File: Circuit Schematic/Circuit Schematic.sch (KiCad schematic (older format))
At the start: 7 parts, among them M1 Motor_Servo, M2 Motor_Servo, U1 SM5420E, U2 SM5420E, U3 ABPDJJ

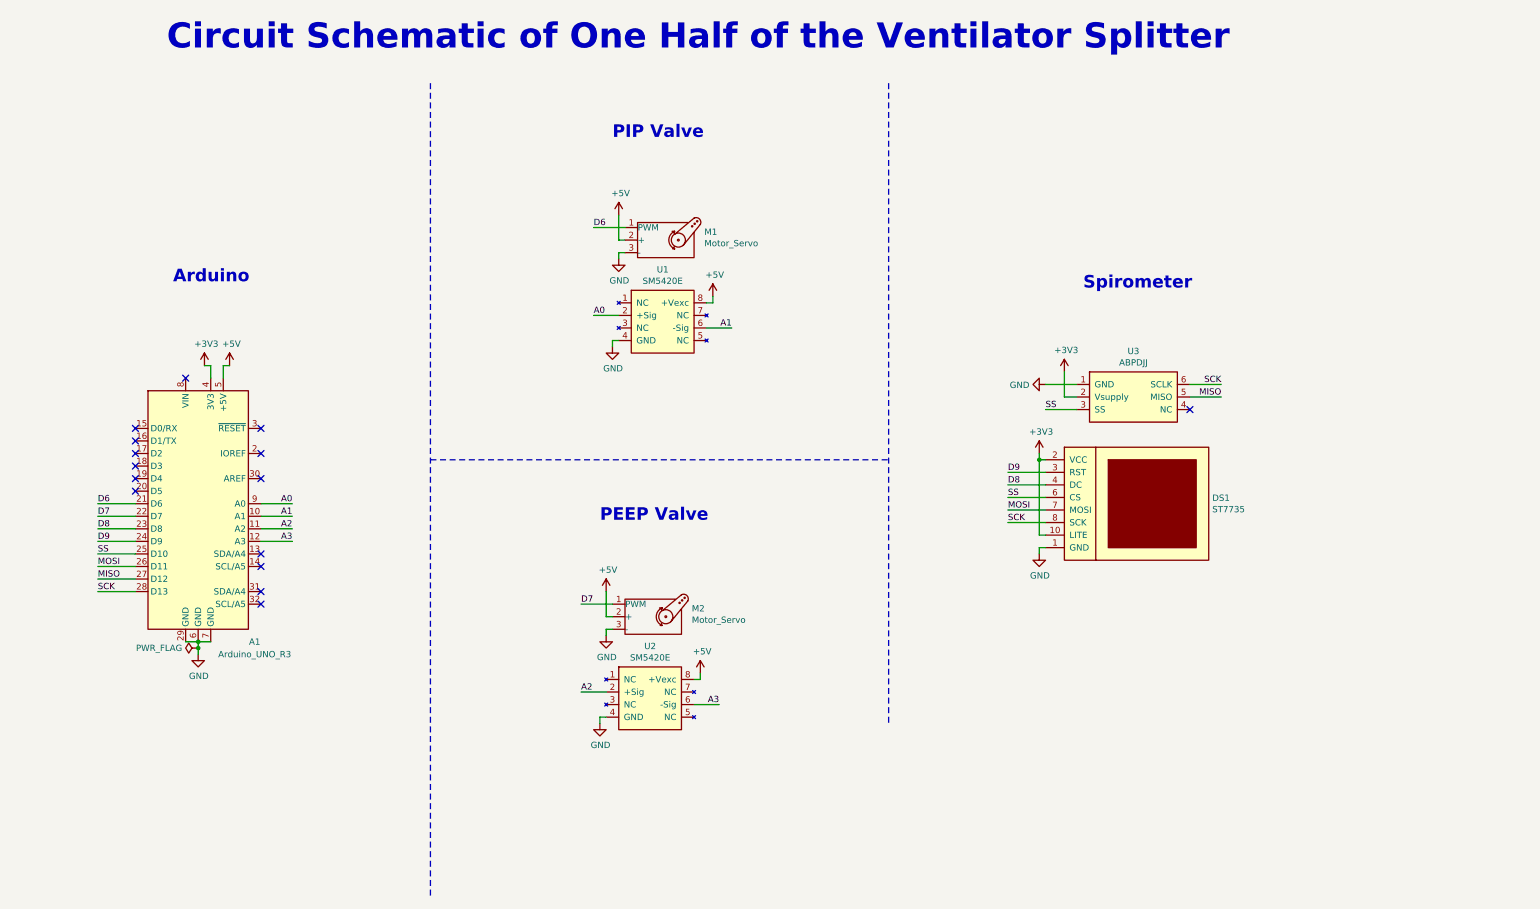
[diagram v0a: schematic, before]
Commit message: Updates schematic to include bluetooth module and alarm system components
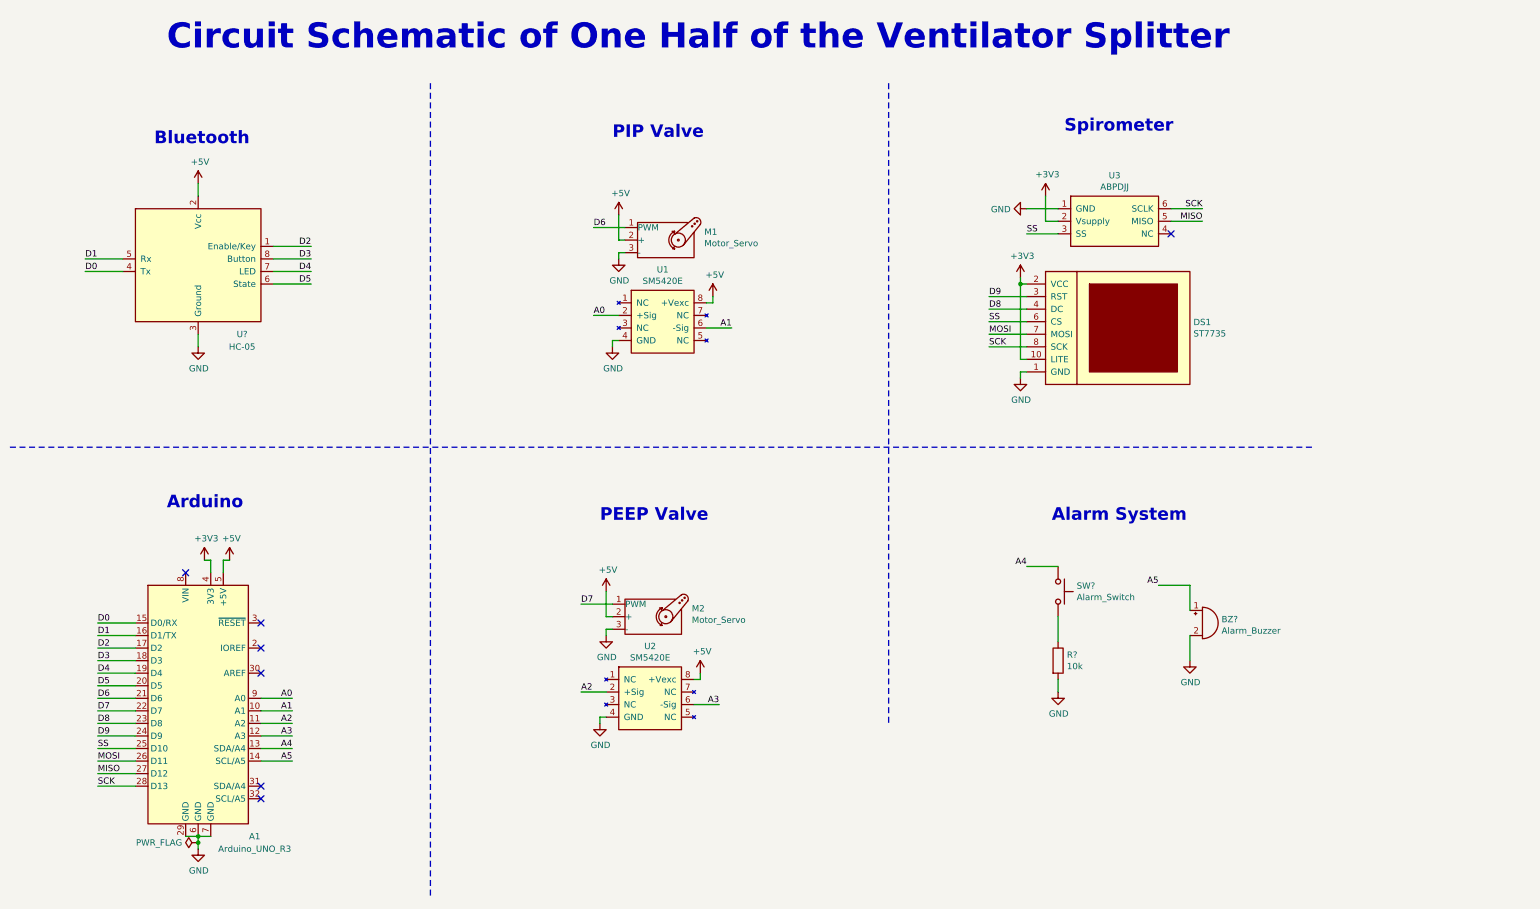
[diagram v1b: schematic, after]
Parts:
- added BZ?: Alarm_Buzzer, symbol Device:Buzzer
- added R?: 10k, symbol Device:R
- added SW?: Alarm_Switch, symbol Switch:SW_Push
- added U?: HC-05, symbol Ventilator-Splitter:HC-05
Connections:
- net +5V: now also U?.2 (Vcc)
- net GND: now also BZ?.2 (+), R?.2, U?.3 (Ground)
- net A4: now reaches A1.13 (SDA/A4)
- net A4: now also SW?.1
- net A5: now reaches A1.14 (SCL/A5)
- net A5: now also BZ?.1 (-)
- net D0: now reaches A1.15 (D0/RX)
- net D0: now also U?.4 (Tx)
- net D1: now reaches A1.16 (D1/TX)
- net D1: now also U?.5 (Rx)
- net D2: now reaches A1.17 (D2)
- net D2: now also U?.1 (Enable/Key)
- net D3: now reaches A1.18 (D3)
- net D3: now also U?.8 (Button)
- net D4: now reaches A1.19 (D4)
- net D4: now also U?.7 (LED)
- net D5: now reaches A1.20 (D5)
- net D5: now also U?.6 (State)
- new net: R?.1, SW?.2
- no-connect marks 15 -> 7
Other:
- note added: "Alarm System"
- note added: "Bluetooth"
- moved on the sheet: A1, DS1, U3

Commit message: Updated buzzer connections
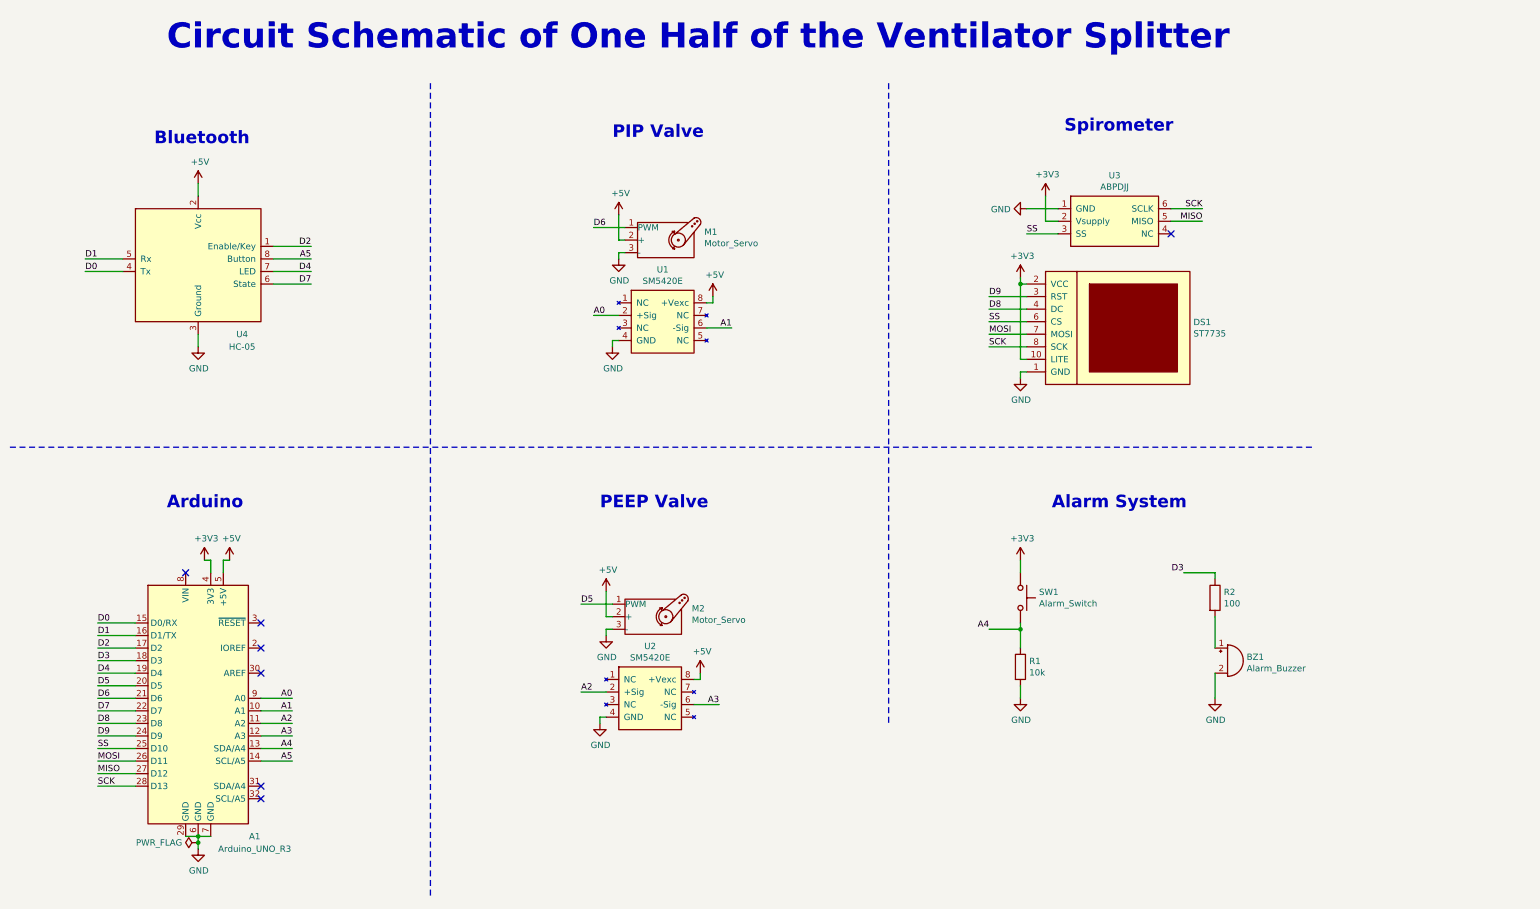
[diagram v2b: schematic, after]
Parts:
- added R2: 100, symbol Device:R
- gave numbers to parts that had none: 4
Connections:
- net +3V3: now also SW1.1
- net A4: now also R1.1, SW1.2; no longer SW1.1
- net A5: now also U4.8 (Button); no longer BZ1.1 (-)
- net D3: now also R2.1; no longer U4.8 (Button)
- net D5: now also M2.1 (PWM); no longer U4.6 (State)
- net D7: now also U4.6 (State); no longer M2.1 (PWM)
- new net: BZ1.1 (-), R2.2
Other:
- moved on the sheet: BZ1, R1, SW1
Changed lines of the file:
@@
 Text Label 1300 6100 0    50   ~ 0
 D6
-Text Label 5150 5350 0    50   ~ 0
+Text Label 3000 2800 2    50   ~ 0
 D7
 Text Label 5250 2350 0    50   ~ 0
@@
 Text Notes 5400 1650 0    100  ~ 20
 PIP Valve
-Text Notes 5300 4700 0    100  ~ 20
+Text Notes 5300 4600 0    100  ~ 20
 PEEP Valve
 Text Notes 9000 1600 0    100  ~ 20
 Spirometer
 $Comp
-L Ventilator-Splitter:HC-05 U?
+L Ventilator-Splitter:HC-05 U4
 U 1 1 5F579D98
 P 2100 3300
-F 0 "U?" H 2450 3400 50  0000 C CNN
+F 0 "U4" H 2450 3400 50  0000 C CNN
 F 1 "HC-05" H 2450 3300 50  0000 C CNN
 F 2 "" H 2100 3300 50  0001 C CNN
@@
 $EndComp
 $Comp
-L power:+5V #PWR?
+L power:+5V #PWR01
 U 1 1 5F57A7E7
 P 2100 2000
-F 0 "#PWR?" H 2100 1850 50  0001 C CNN
+F 0 "#PWR01" H 2100 1850 50  0001 C CNN
 F 1 "+5V" H 2115 2173 50  0000 C CNN
 F 2 "" H 2100 2000 50  0001 C CNN
@@
 $EndComp
 $Comp
-L power:GND #PWR?
+L power:GND #PWR02
 U 1 1 5F57B6FB
 P 2100 3300
-F 0 "#PWR?" H 2100 3050 50  0001 C CNN
+F 0 "#PWR02" H 2100 3050 50  0001 C CNN
 F 1 "GND" H 2105 3127 50  0000 C CNN
 F 2 "" H 2100 3300 50  0001 C CNN
@@
 Wire Wire Line
 	2700 2600 3000 2600
-Text Label 3000 2600 2    50   ~ 0
+Text Label 9950 5100 2    50   ~ 0
 D3
 Wire Wire Line
@@
 Wire Wire Line
 	2700 2800 3000 2800
-Text Label 3000 2800 2    50   ~ 0
+Text Label 5150 5350 0    50   ~ 0
 D5
 Wire Wire Line
@@
 Bluetooth
 $Comp
-L Device:Buzzer BZ?
+L Device:Buzzer BZ1
 U 1 1 5F5A77D7
-P 10100 5500
-F 0 "BZ?" H 10252 5529 50  0000 L CNN
-F 1 "Alarm_Buzzer" H 10252 5438 50  0000 L CNN
-F 2 "" V 10075 5600 50  0001 C CNN
-F 3 "~" V 10075 5600 50  0001 C CNN
-	1    10100 5500
-	1    0    0    -1
-$EndComp
-$Comp
-L Device:R R?
+P 10300 5800
+F 0 "BZ1" H 10452 5829 50  0000 L CNN
+F 1 "Alarm_Buzzer" H 10452 5738 50  0000 L CNN
+F 2 "" V 10275 5900 50  0001 C CNN
+F 3 "~" V 10275 5900 50  0001 C CNN
+	1    10300 5800
+	1    0    0    -1
+$EndComp
+$Comp
+L Device:R R1
 U 1 1 5F5A8DAE
-P 8950 5800
-F 0 "R?" H 9020 5846 50  0000 L CNN
-F 1 "10k" H 9020 5755 50  0000 L CNN
-F 2 "" V 8880 5800 50  0001 C CNN
-F 3 "~" H 8950 5800 50  0001 C CNN
-	1    8950 5800
-	1    0    0    -1
-$EndComp
-$Comp
-L Switch:SW_Push SW?
+P 8650 5850
+F 0 "R1" H 8720 5896 50  0000 L CNN
+F 1 "10k" H 8720 5805 50  0000 L CNN
+F 2 "" V 8580 5850 50  0001 C CNN
+F 3 "~" H 8650 5850 50  0001 C CNN
+	1    8650 5850
+	1    0    0    -1
+$EndComp
+$Comp
+L Switch:SW_Push SW1
 U 1 1 5F5A800E
-P 8950 5250
-F 0 "SW?" V 8904 5398 50  0000 L CNN
-F 1 "Alarm_Switch" V 8995 5398 50  0000 L CNN
-F 2 "" H 8950 5450 50  0001 C CNN
-F 3 "~" H 8950 5450 50  0001 C CNN
-	1    8950 5250
+P 8650 5300
+F 0 "SW1" V 8604 5448 50  0000 L CNN
+F 1 "Alarm_Switch" V 8695 5448 50  0000 L CNN
+F 2 "" H 8650 5500 50  0001 C CNN
+F 3 "~" H 8650 5500 50  0001 C CNN
+	1    8650 5300
 	0    1    1    0
 $EndComp
@@
 A5
 Wire Wire Line
-	8700 5050 8950 5050
-Wire Wire Line
-	9750 5200 10000 5200
-Text Label 8700 5050 2    50   ~ 0
+	8400 5550 8650 5550
+Wire Wire Line
+	9950 5100 10200 5100
+Text Label 8400 5550 2    50   ~ 0
 A4
-Text Label 9750 5200 2    50   ~ 0
+Text Label 3000 2600 2    50   ~ 0
 A5
 Wire Wire Line
-	8950 5450 8950 5650
-Wire Wire Line
-	8950 5950 8950 6050
-Wire Wire Line
-	10000 5200 10000 5400
-$Comp
-L power:GND #PWR?
+	8650 5500 8650 5550
+Wire Wire Line
+	8650 6000 8650 6100
+$Comp
+L power:GND #PWR03
 U 1 1 5F5CC3F3
-P 8950 6050
-F 0 "#PWR?" H 8950 5800 50  0001 C CNN
-F 1 "GND" H 8955 5877 50  0000 C CNN
-F 2 "" H 8950 6050 50  0001 C CNN
-F 3 "" H 8950 6050 50  0001 C CNN
-	1    8950 6050
-	1    0    0    -1
-$EndComp
-Text Notes 8900 4700 0    100  ~ 20
+P 8650 6100
+F 0 "#PWR03" H 8650 5850 50  0001 C CNN
+F 1 "GND" H 8655 5927 50  0000 C CNN
+F 2 "" H 8650 6100 50  0001 C CNN
+F 3 "" H 8650 6100 50  0001 C CNN
+	1    8650 6100
+	1    0    0    -1
+$EndComp
+Text Notes 8900 4600 0    100  ~ 20
 Alarm System
 Wire Notes Line
 	600  4100 11000 4100
 $Comp
-L power:GND #PWR?
+L power:GND #PWR04
 U 1 1 5F5CC6D4
-P 10000 5800
-F 0 "#PWR?" H 10000 5550 50  0001 C CNN
-F 1 "GND" H 10005 5627 50  0000 C CNN
-F 2 "" H 10000 5800 50  0001 C CNN
-F 3 "" H 10000 5800 50  0001 C CNN
-	1    10000 5800
-	1    0    0    -1
-$EndComp
-Wire Wire Line
-	10000 5600 10000 5800
+P 10200 6100
+F 0 "#PWR04" H 10200 5850 50  0001 C CNN
+F 1 "GND" H 10205 5927 50  0000 C CNN
+F 2 "" H 10200 6100 50  0001 C CNN
+F 3 "" H 10200 6100 50  0001 C CNN
+	1    10200 6100
+	1    0    0    -1
+$EndComp
+Wire Wire Line
+	10200 5900 10200 6100
+$Comp
+L Device:R R2
+U 1 1 5F575512
+P 10200 5300
+F 0 "R2" H 10270 5346 50  0000 L CNN
+F 1 "100" H 10270 5255 50  0000 L CNN
+F 2 "" V 10130 5300 50  0001 C CNN
+F 3 "~" H 10200 5300 50  0001 C CNN
+	1    10200 5300
+	1    0    0    -1
+$EndComp
+Wire Wire Line
+	10200 5100 10200 5150
+Wire Wire Line
+	10200 5450 10200 5700
+Connection ~ 8650 5550
+Wire Wire Line
+	8650 5550 8650 5700
+$Comp
+L power:+3V3 #PWR?
+U 1 1 5F56E1A1
+P 8650 5000
+F 0 "#PWR?" H 8650 4850 50  0001 C CNN
+F 1 "+3V3" H 8665 5173 50  0000 C CNN
+F 2 "" H 8650 5000 50  0001 C CNN
+F 3 "" H 8650 5000 50  0001 C CNN
+	1    8650 5000
+	1    0    0    -1
+$EndComp
+Wire Wire Line
+	8650 5000 8650 5100
 $EndSCHEMATC
